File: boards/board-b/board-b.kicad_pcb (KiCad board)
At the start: 2 copper layers, 110 x 85 mm, 86 parts, among them J10 DW254P-2X8-L0, J11 DW254P-2X8-L0, J5 PM254V-11-06-H85, J6 WJ500V-5.08-2P, J7 WJ500V-5.08-2P, P1 ATT/PDOK pads, U2 AP63201WU-7, U3 LM2596S-ADJ, U4 LM2596S-ADJ, U6 LT1963AEQ#PBF, U7 LT1963AEQ#PBF, U8 LT3015EQ-12#PBF

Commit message: feat(board-b): add back silkscreen artwork and tooling
New scripts apply silkscreen artwork to board B rear copper, with evidence rebinding for regenerated designs.

Co-Authored-By: Claude Fable 5.1 <noreply@anthropic.com>
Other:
- board text added: "+12V : 1.2A"
- board text added: "+5V : 0.5A"
- board text added: "-12V : 0.8A"
- board text added: "zudo-pd v1"
- board text removed: "zudo-pd B / rev1"

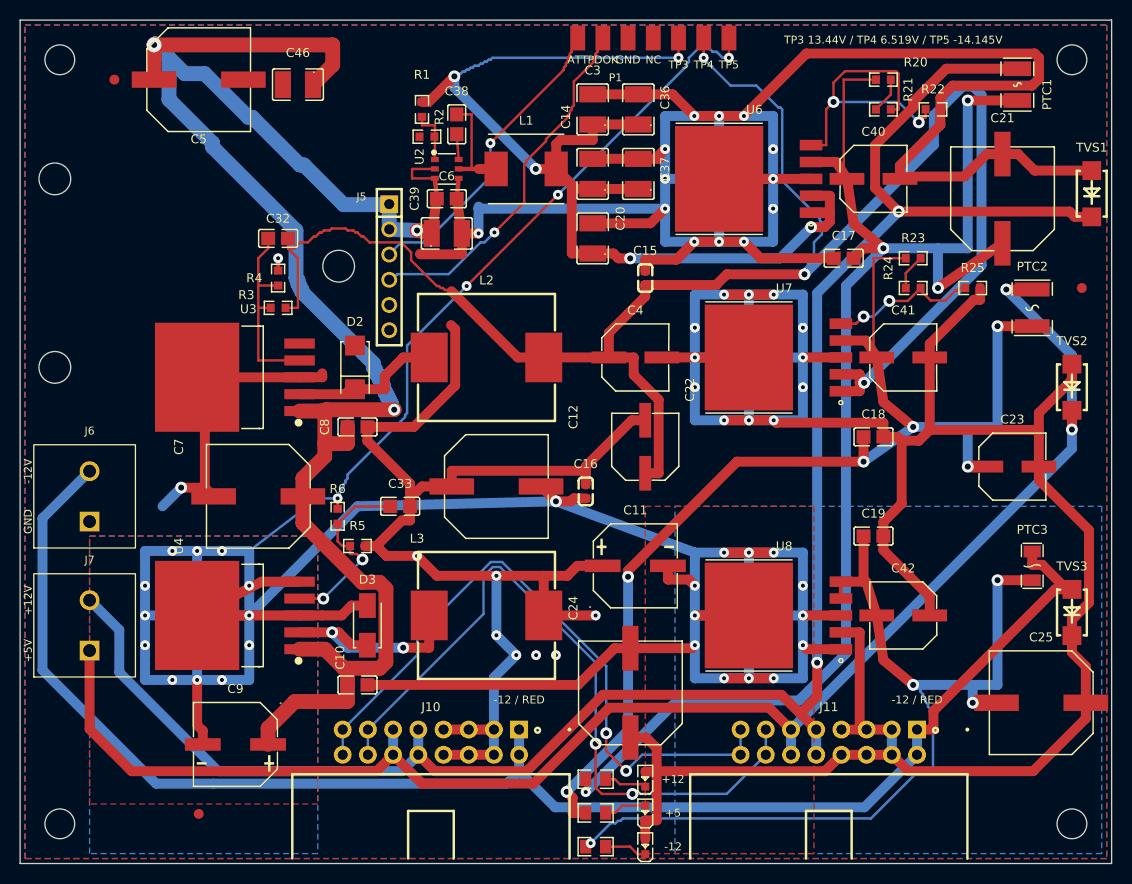
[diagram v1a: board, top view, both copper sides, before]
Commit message: fix(board-b): replace out-of-stock LDOs, add U8 ADJ divider, correct LED2 polarity
Replace U6/U7 LT1963AEQ#PBF (C107286) with LT1963AEQ#TRPBF (C459702);
U8 fixed LT3015EQ-12#PBF (C666307) with adjustable LT3015EQ#PBF (C666306)
and new R26/R27/R28 divider (nominal −12.054 V). Also: LED2 (C2289) symbol
pin numbering corrected to pin 1 = cathode per LCSC library and footprint
turned 180° with copper unchanged (JLCPCB preview showed it reversed);
front/back silkscreen tidied; P1 label rule in verify-compact-mechanics.py relaxed
to nearest-own-contact.

Co-Authored-By: Claude Fable 5.1 <noreply@anthropic.com>
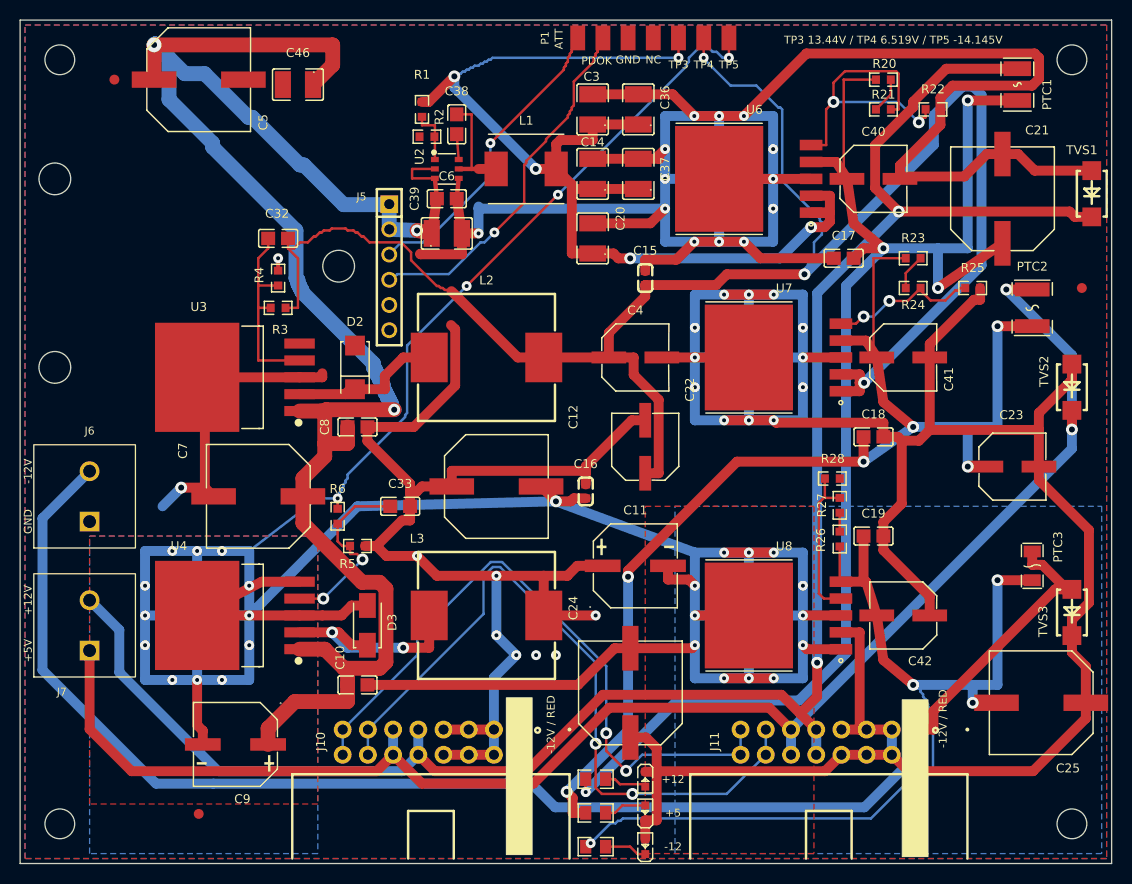
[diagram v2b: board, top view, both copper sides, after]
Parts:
- added R26: 8200R 0.1%, zudo-pd:R0603, F.Cu at (82.6, 52.3)
- added R27: 680R 0.1%, zudo-pd:R0603, F.Cu at (82.6, 48.9)
- added R28: 1000R 0.1%, zudo-pd:R0603, F.Cu at (81.8, 46.2)
- U6, U7: value LT1963AEQ#PBF -> LT1963AEQ#TRPBF
- U8: value LT3015EQ-12#PBF -> LT3015EQ#PBF
- turned LED2 to -90 degrees
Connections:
- LED2 pad 1: Net-(R7-LED2) -> GND
- LED2 pad 2: GND -> Net-(R7-LED2)
- U8 pad 4: Net-(U8-OUT) -> U8 ADJ
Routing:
- net U8 ADJ: track 0.00 -> 15.8 mm
- net U8 FB upper series: track 0.00 -> 1.90 mm
- net Net-(U8-OUT): track 95.4 -> 97.3 mm
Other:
- board text added: "-12V / RED"
- board text removed: "-12 / RED"
